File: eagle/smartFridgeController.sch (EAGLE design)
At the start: 12 parts

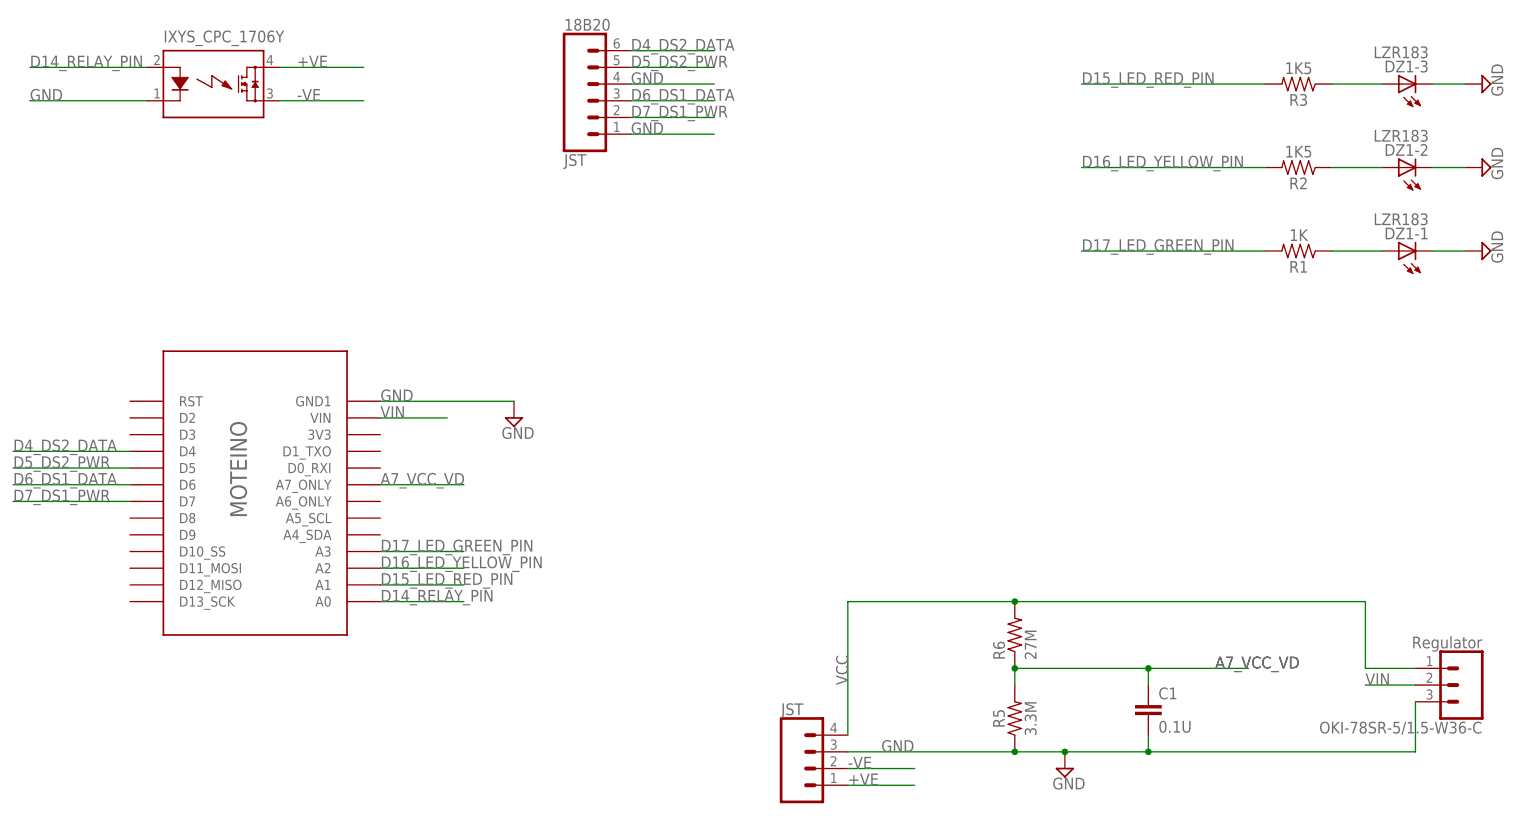
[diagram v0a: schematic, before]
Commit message: added RGB LED
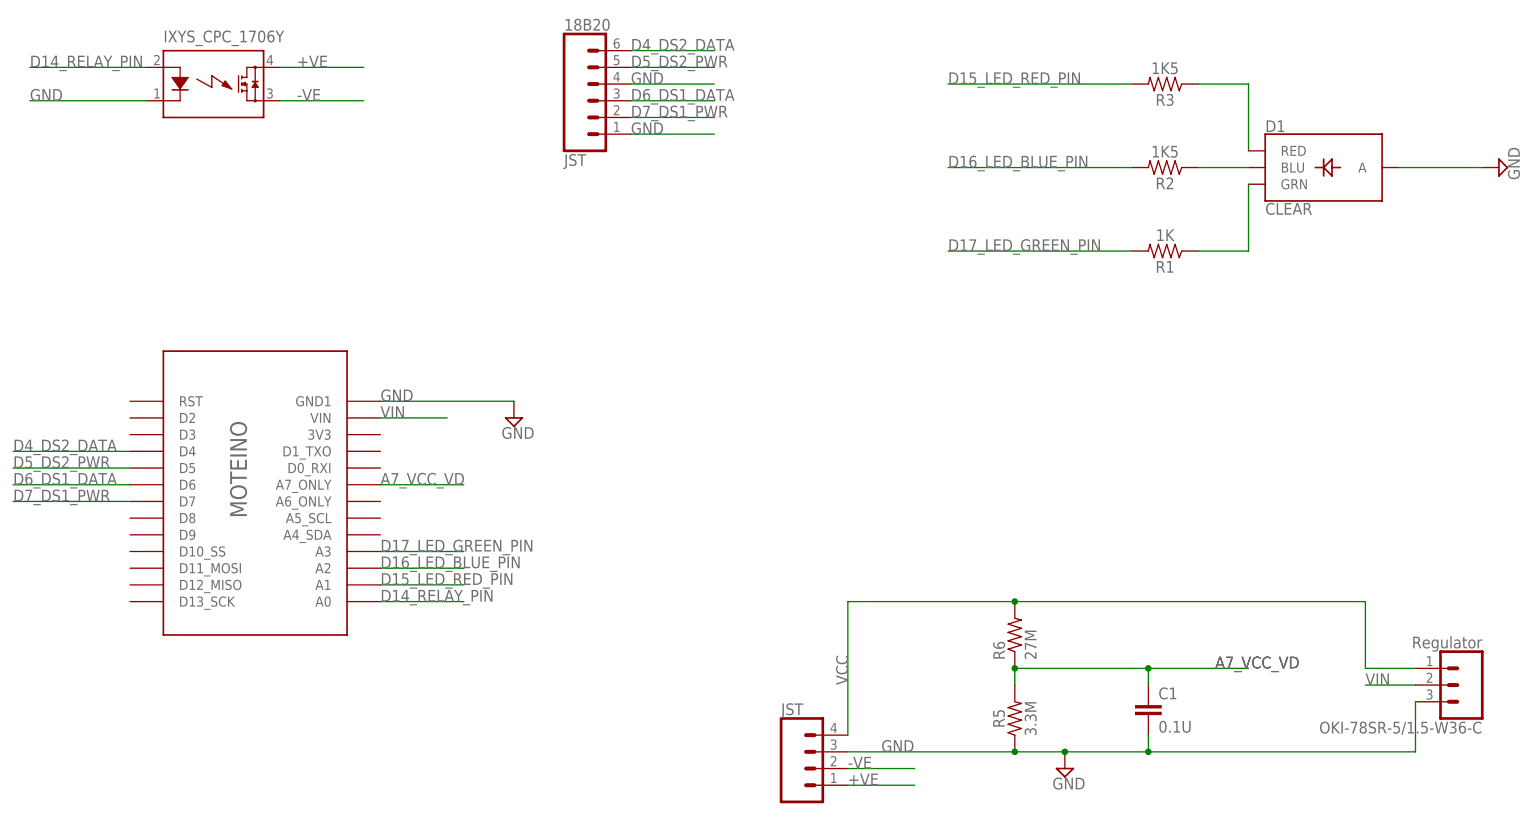
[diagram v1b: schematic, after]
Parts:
- removed DZ1: LZR183, led:LZR183
- added D1: CLEAR, SparkFun-LED:LED-RGB-CACLEAR
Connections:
- net D16_LED_YELLOW_PIN renamed D16_LED_BLUE_PIN
- net GND: no longer DZ1-1.C, DZ1-2.C, DZ1-3.C
- net N$1: now also D1.RED, R3.1; no longer DZ1-1.A, R1.1
- net N$2: now also D1.BLU; no longer DZ1-2.A
- net N$3: now also D1.GRN, R1.1; no longer DZ1-3.A, R3.1
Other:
- moved on the sheet: R1, R2, R3
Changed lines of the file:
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@@
 <part name="OKI-78SR-5/1.5-W36-C" library="SparkFun-Connectors" deviceset="CONN_03" device="" value="Regulator"/>
 <part name="18B20" library="SparkFun-Connectors" deviceset="CONN_06" device="SILK_FEMALE_PTH" value="JST"/>
-<part name="DZ1" library="led" library_urn="urn:adsk.eagle:library:259" deviceset="LZR183" device="" package3d_urn="urn:adsk.eagle:package:15788/1"/>
 <part name="R1" library="SparkFun-Resistors" deviceset="1KOHM" device="-HORIZ-1/4W-1%" value="1K"/>
 <part name="R2" library="SparkFun-Resistors" deviceset="1KOHM" device="-HORIZ-1/4W-1%" value="1K5"/>
 <part name="R3" library="SparkFun-Resistors" deviceset="1KOHM" device="-HORIZ-1/4W-1%" value="1K5"/>
 <part name="SUPPLY1" library="supply2" deviceset="GND" device=""/>
-<part name="SUPPLY2" library="supply2" deviceset="GND" device=""/>
-<part name="SUPPLY4" library="supply2" deviceset="GND" device=""/>
 <part name="U$2" library="Moteino" deviceset="MOTEINO_SIMPLE" device=""/>
 <part name="IXYS_CPC_1706Y" library="relay" library_urn="urn:adsk.eagle:library:339" deviceset="AQZ10*D" device="" package3d_urn="urn:adsk.eagle:package:24370/1" technology="2"/>
+<part name="D1" library="SparkFun-LED" deviceset="LED-RGB-CA" device="CLEAR" value="CLEAR"/>
 </parts>
 <sheets>
@@
 <instance part="OKI-78SR-5/1.5-W36-C" gate="J$1" x="238.76" y="55.88" rot="R180"/>
 <instance part="18B20" gate="G$1" x="106.68" y="144.78"/>
-<instance part="DZ1" gate="-1" x="228.6" y="121.92" rot="R90"/>
-<instance part="DZ1" gate="-2" x="228.6" y="134.62" rot="R90"/>
-<instance part="DZ1" gate="-3" x="228.6" y="147.32" rot="R90"/>
-<instance part="R1" gate="G$1" x="213.36" y="121.92" rot="R180"/>
-<instance part="R2" gate="G$1" x="213.36" y="134.62" rot="R180"/>
-<instance part="R3" gate="G$1" x="213.36" y="147.32" rot="R180"/>
-<instance part="SUPPLY1" gate="GND" x="241.3" y="121.92" rot="R90"/>
-<instance part="SUPPLY2" gate="GND" x="241.3" y="134.62" rot="R90"/>
-<instance part="SUPPLY4" gate="GND" x="241.3" y="147.32" rot="R90"/>
+<instance part="R1" gate="G$1" x="193.04" y="121.92" rot="R180"/>
+<instance part="R2" gate="G$1" x="193.04" y="134.62" rot="R180"/>
+<instance part="R3" gate="G$1" x="193.04" y="147.32" rot="R180"/>
+<instance part="SUPPLY1" gate="GND" x="243.84" y="134.62" rot="R90"/>
 <instance part="U$2" gate="G$1" x="50.8" y="81.28"/>
 <instance part="IXYS_CPC_1706Y" gate="G$1" x="48.26" y="147.32" smashed="yes">
 <attribute name="NAME" x="40.64" y="153.67" size="1.778" layer="95" font="vector"/>
 </instance>
+<instance part="D1" gate="G$1" x="215.9" y="134.62"/>
 </instances>
 <busses>
@@
 </segment>
 <segment>
-<pinref part="DZ1" gate="-1" pin="C"/>
-<wire x1="233.68" y1="121.92" x2="238.76" y2="121.92" width="0.1524" layer="91"/>
+<wire x1="228.6" y1="134.62" x2="241.3" y2="134.62" width="0.1524" layer="91"/>
 <pinref part="SUPPLY1" gate="GND" pin="GND"/>
-</segment>
-<segment>
-<pinref part="DZ1" gate="-2" pin="C"/>
-<wire x1="233.68" y1="134.62" x2="238.76" y2="134.62" width="0.1524" layer="91"/>
-<pinref part="SUPPLY2" gate="GND" pin="GND"/>
-</segment>
-<segment>
-<pinref part="DZ1" gate="-3" pin="C"/>
-<wire x1="233.68" y1="147.32" x2="238.76" y2="147.32" width="0.1524" layer="91"/>
-<pinref part="SUPPLY4" gate="GND" pin="GND"/>
 </segment>
 <segment>
@@
 <segment>
 <pinref part="R3" gate="G$1" pin="2"/>
-<wire x1="208.28" y1="147.32" x2="180.34" y2="147.32" width="0.1524" layer="91"/>
-<label x="180.34" y="147.32" size="1.778" layer="95"/>
+<wire x1="187.96" y1="147.32" x2="160.02" y2="147.32" width="0.1524" layer="91"/>
+<label x="160.02" y="147.32" size="1.778" layer="95"/>
 </segment>
 </net>
@@
 <wire x1="111.76" y1="149.86" x2="124.46" y2="149.86" width="0.1524" layer="91"/>
 <label x="111.76" y="149.86" size="1.778" layer="95"/>
-</segment>
-</net>
-<net name="N$1" class="0">
-<segment>
-<pinref part="R1" gate="G$1" pin="1"/>
-<pinref part="DZ1" gate="-1" pin="A"/>
-<wire x1="218.44" y1="121.92" x2="226.06" y2="121.92" width="0.1524" layer="91"/>
-</segment>
-</net>
-<net name="N$2" class="0">
-<segment>
-<pinref part="R2" gate="G$1" pin="1"/>
-<pinref part="DZ1" gate="-2" pin="A"/>
-<wire x1="218.44" y1="134.62" x2="226.06" y2="134.62" width="0.1524" layer="91"/>
-</segment>
-</net>
-<net name="N$3" class="0">
-<segment>
-<pinref part="R3" gate="G$1" pin="1"/>
-<pinref part="DZ1" gate="-3" pin="A"/>
-<wire x1="218.44" y1="147.32" x2="226.06" y2="147.32" width="0.1524" layer="91"/>
 </segment>
 </net>
@@
 </segment>
 </net>
-<net name="D16_LED_YELLOW_PIN" class="0">
+<net name="D17_LED_GREEN_PIN" class="0">
+<segment>
+<wire x1="73.66" y1="76.2" x2="86.36" y2="76.2" width="0.1524" layer="91"/>
+<label x="73.66" y="76.2" size="1.778" layer="95"/>
+<pinref part="U$2" gate="G$1" pin="A3"/>
+</segment>
+<segment>
+<pinref part="R1" gate="G$1" pin="2"/>
+<wire x1="187.96" y1="121.92" x2="160.02" y2="121.92" width="0.1524" layer="91"/>
+<label x="160.02" y="121.92" size="1.778" layer="95"/>
+</segment>
+</net>
+<net name="N$1" class="0">
+<segment>
+<pinref part="R3" gate="G$1" pin="1"/>
+<pinref part="D1" gate="G$1" pin="RED"/>
+<wire x1="198.12" y1="147.32" x2="205.74" y2="147.32" width="0.1524" layer="91"/>
+<wire x1="205.74" y1="147.32" x2="205.74" y2="137.16" width="0.1524" layer="91"/>
+</segment>
+</net>
+<net name="N$2" class="0">
+<segment>
+<pinref part="R2" gate="G$1" pin="1"/>
+<pinref part="D1" gate="G$1" pin="BLU"/>
+<wire x1="198.12" y1="134.62" x2="205.74" y2="134.62" width="0.1524" layer="91"/>
+</segment>
+</net>
+<net name="N$3" class="0">
+<segment>
+<pinref part="R1" gate="G$1" pin="1"/>
+<pinref part="D1" gate="G$1" pin="GRN"/>
+<wire x1="198.12" y1="121.92" x2="205.74" y2="121.92" width="0.1524" layer="91"/>
+<wire x1="205.74" y1="121.92" x2="205.74" y2="132.08" width="0.1524" layer="91"/>
+</segment>
+</net>
+<net name="D16_LED_BLUE_PIN" class="0">
+<segment>
+<pinref part="R2" gate="G$1" pin="2"/>
+<wire x1="187.96" y1="134.62" x2="160.02" y2="134.62" width="0.1524" layer="91"/>
+<label x="160.02" y="134.62" size="1.778" layer="95"/>
+</segment>
 <segment>
 <wire x1="73.66" y1="73.66" x2="86.36" y2="73.66" width="0.1524" layer="91"/>
@@
 <pinref part="U$2" gate="G$1" pin="A2"/>
 </segment>
-<segment>
-<pinref part="R2" gate="G$1" pin="2"/>
-<wire x1="208.28" y1="134.62" x2="180.34" y2="134.62" width="0.1524" layer="91"/>
-<label x="180.34" y="134.62" size="1.778" layer="95"/>
-</segment>
-</net>
-<net name="D17_LED_GREEN_PIN" class="0">
-<segment>
-<wire x1="73.66" y1="76.2" x2="86.36" y2="76.2" width="0.1524" layer="91"/>
-<label x="73.66" y="76.2" size="1.778" layer="95"/>
-<pinref part="U$2" gate="G$1" pin="A3"/>
-</segment>
-<segment>
-<pinref part="R1" gate="G$1" pin="2"/>
-<wire x1="208.28" y1="121.92" x2="180.34" y2="121.92" width="0.1524" layer="91"/>
-<label x="180.34" y="121.92" size="1.778" layer="95"/>
-</segment>
-</net>
+</net>

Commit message: simpler route, gnd pour
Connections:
- removed net D14_RELAY_PIN: IXYS_CPC_1706Y.A, U$2.A0
- removed net D15_LED_RED_PIN: R3.2, U$2.A1
- removed net D17_LED_GREEN_PIN: R1.2, U$2.A3
- new net D14_LED_RED_PIN: R3.2, U$2.A0
- new net D15_LED_GREEN_PIN: R1.2, U$2.A1
- new net D17_RELAY_PIN: IXYS_CPC_1706Y.A, U$2.A3
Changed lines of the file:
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@@
 </segment>
 </net>
-<net name="D15_LED_RED_PIN" class="0">
-<segment>
-<wire x1="73.66" y1="71.12" x2="86.36" y2="71.12" width="0.1524" layer="91"/>
-<label x="73.66" y="71.12" size="1.778" layer="95"/>
-<pinref part="U$2" gate="G$1" pin="A1"/>
-</segment>
+<net name="D14_LED_RED_PIN" class="0">
 <segment>
 <pinref part="R3" gate="G$1" pin="2"/>
 <wire x1="187.96" y1="147.32" x2="160.02" y2="147.32" width="0.1524" layer="91"/>
 <label x="160.02" y="147.32" size="1.778" layer="95"/>
+</segment>
+<segment>
+<pinref part="U$2" gate="G$1" pin="A0"/>
+<wire x1="73.66" y1="68.58" x2="86.36" y2="68.58" width="0.1524" layer="91"/>
+<label x="73.66" y="68.58" size="1.778" layer="95"/>
 </segment>
 </net>
@@
 </segment>
 </net>
-<net name="D14_RELAY_PIN" class="0">
-<segment>
-<wire x1="73.66" y1="68.58" x2="86.36" y2="68.58" width="0.1524" layer="91"/>
-<label x="73.66" y="68.58" size="1.778" layer="95"/>
-<pinref part="U$2" gate="G$1" pin="A0"/>
-</segment>
+<net name="D17_RELAY_PIN" class="0">
 <segment>
 <wire x1="38.1" y1="149.86" x2="20.32" y2="149.86" width="0.1524" layer="91"/>
@@
 <pinref part="IXYS_CPC_1706Y" gate="G$1" pin="A"/>
 </segment>
-</net>
-<net name="D17_LED_GREEN_PIN" class="0">
 <segment>
+<pinref part="U$2" gate="G$1" pin="A3"/>
 <wire x1="73.66" y1="76.2" x2="86.36" y2="76.2" width="0.1524" layer="91"/>
 <label x="73.66" y="76.2" size="1.778" layer="95"/>
-<pinref part="U$2" gate="G$1" pin="A3"/>
-</segment>
-<segment>
-<pinref part="R1" gate="G$1" pin="2"/>
-<wire x1="187.96" y1="121.92" x2="160.02" y2="121.92" width="0.1524" layer="91"/>
-<label x="160.02" y="121.92" size="1.778" layer="95"/>
 </segment>
 </net>
@@
 </segment>
 <segment>
+<pinref part="U$2" gate="G$1" pin="A2"/>
 <wire x1="73.66" y1="73.66" x2="86.36" y2="73.66" width="0.1524" layer="91"/>
 <label x="73.66" y="73.66" size="1.778" layer="95"/>
-<pinref part="U$2" gate="G$1" pin="A2"/>
 </segment>
 </net>
+<net name="D15_LED_GREEN_PIN" class="0">
+<segment>
+<pinref part="R1" gate="G$1" pin="2"/>
+<wire x1="187.96" y1="121.92" x2="160.02" y2="121.92" width="0.1524" layer="91"/>
+<label x="160.02" y="121.92" size="1.778" layer="95"/>
+</segment>
+<segment>
+<pinref part="U$2" gate="G$1" pin="A1"/>
+<wire x1="73.66" y1="71.12" x2="86.36" y2="71.12" width="0.1524" layer="91"/>
+<label x="73.66" y="71.12" size="1.778" layer="95"/>
+</segment>
+</net>

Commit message: New layout, 0.3
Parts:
- JST: value (none) -> 18B20
- renumbered D1 to STATUS_LED
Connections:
- net GND: now also STATUS_LED.A
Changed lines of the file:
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@@
 <part name="C1" library="SparkFun-Capacitors" deviceset="0.1UF" device="-KIT-EZ-50V-20%" value="0.1U"/>
 <part name="R5" library="SparkFun-Resistors" deviceset="1KOHM" device="-HORIZ-1/4W-1%" value="3.3M"/>
-<part name="JST" library="SparkFun-Connectors" deviceset="CONN_04" device="JST-PTH"/>
+<part name="JST" library="SparkFun-Connectors" deviceset="CONN_04" device="JST-PTH" value="18B20"/>
 <part name="R6" library="adafruit" deviceset="R-US_" device="0309/12" value="27M"/>
 <part name="SUPPLY3" library="supply2" deviceset="GND" device=""/>
@@
 <part name="U$2" library="Moteino" deviceset="MOTEINO_SIMPLE" device=""/>
 <part name="IXYS_CPC_1706Y" library="relay" library_urn="urn:adsk.eagle:library:339" deviceset="AQZ10*D" device="" package3d_urn="urn:adsk.eagle:package:24370/1" technology="2"/>
-<part name="D1" library="SparkFun-LED" deviceset="LED-RGB-CA" device="CLEAR" value="CLEAR"/>
+<part name="STATUS_LED" library="SparkFun-LED" deviceset="LED-RGB-CA" device="CLEAR" value="CLEAR"/>
 </parts>
 <sheets>
@@
 <attribute name="NAME" x="40.64" y="153.67" size="1.778" layer="95" font="vector"/>
 </instance>
-<instance part="D1" gate="G$1" x="215.9" y="134.62"/>
+<instance part="STATUS_LED" gate="G$1" x="215.9" y="134.62"/>
 </instances>
 <busses>
@@
 </segment>
 <segment>
-<wire x1="228.6" y1="134.62" x2="241.3" y2="134.62" width="0.1524" layer="91"/>
-<pinref part="SUPPLY1" gate="GND" pin="GND"/>
-</segment>
-<segment>
 <wire x1="38.1" y1="144.78" x2="20.32" y2="144.78" width="0.1524" layer="91"/>
 <label x="20.32" y="144.78" size="1.778" layer="95"/>
 <pinref part="IXYS_CPC_1706Y" gate="G$1" pin="K"/>
+</segment>
+<segment>
+<pinref part="STATUS_LED" gate="G$1" pin="A"/>
+<pinref part="SUPPLY1" gate="GND" pin="GND"/>
+<wire x1="228.6" y1="134.62" x2="241.3" y2="134.62" width="0.1524" layer="91"/>
+<label x="228.6" y="134.62" size="1.778" layer="95"/>
 </segment>
 </net>
@@
 <segment>
 <pinref part="R3" gate="G$1" pin="1"/>
-<pinref part="D1" gate="G$1" pin="RED"/>
+<pinref part="STATUS_LED" gate="G$1" pin="RED"/>
 <wire x1="198.12" y1="147.32" x2="205.74" y2="147.32" width="0.1524" layer="91"/>
 <wire x1="205.74" y1="147.32" x2="205.74" y2="137.16" width="0.1524" layer="91"/>
@@
 <segment>
 <pinref part="R2" gate="G$1" pin="1"/>
-<pinref part="D1" gate="G$1" pin="BLU"/>
+<pinref part="STATUS_LED" gate="G$1" pin="BLU"/>
 <wire x1="198.12" y1="134.62" x2="205.74" y2="134.62" width="0.1524" layer="91"/>
 </segment>
@@
 <segment>
 <pinref part="R1" gate="G$1" pin="1"/>
-<pinref part="D1" gate="G$1" pin="GRN"/>
+<pinref part="STATUS_LED" gate="G$1" pin="GRN"/>
 <wire x1="198.12" y1="121.92" x2="205.74" y2="121.92" width="0.1524" layer="91"/>
 <wire x1="205.74" y1="121.92" x2="205.74" y2="132.08" width="0.1524" layer="91"/>
@@
 </sheet>
 </sheets>
-<errors>
-</errors>
 </schematic>
 </drawing>
